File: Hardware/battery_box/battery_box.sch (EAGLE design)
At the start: 24 parts, among them IC1 LM2574N-5.0, U1 PIC16F506P

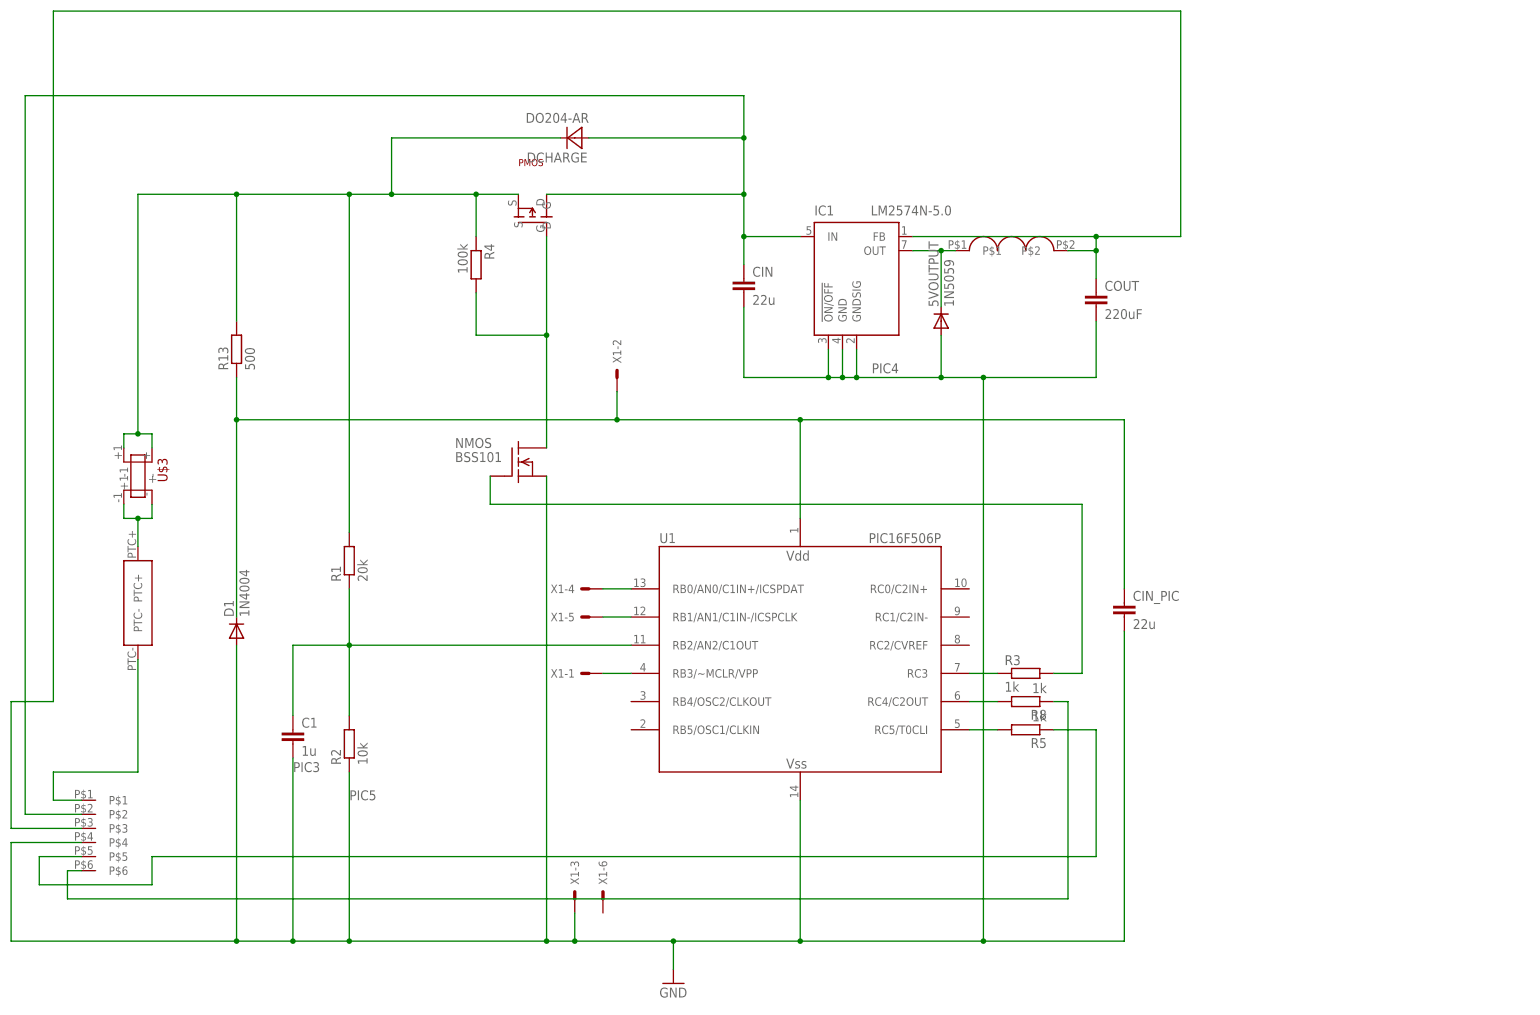
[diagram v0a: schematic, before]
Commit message: Added Connectors to Schematic
Adds the DC Jacks and USB connectors and LEDs to the schematic for
mounting on PCB. Added comments to schematic and changed .gitignore
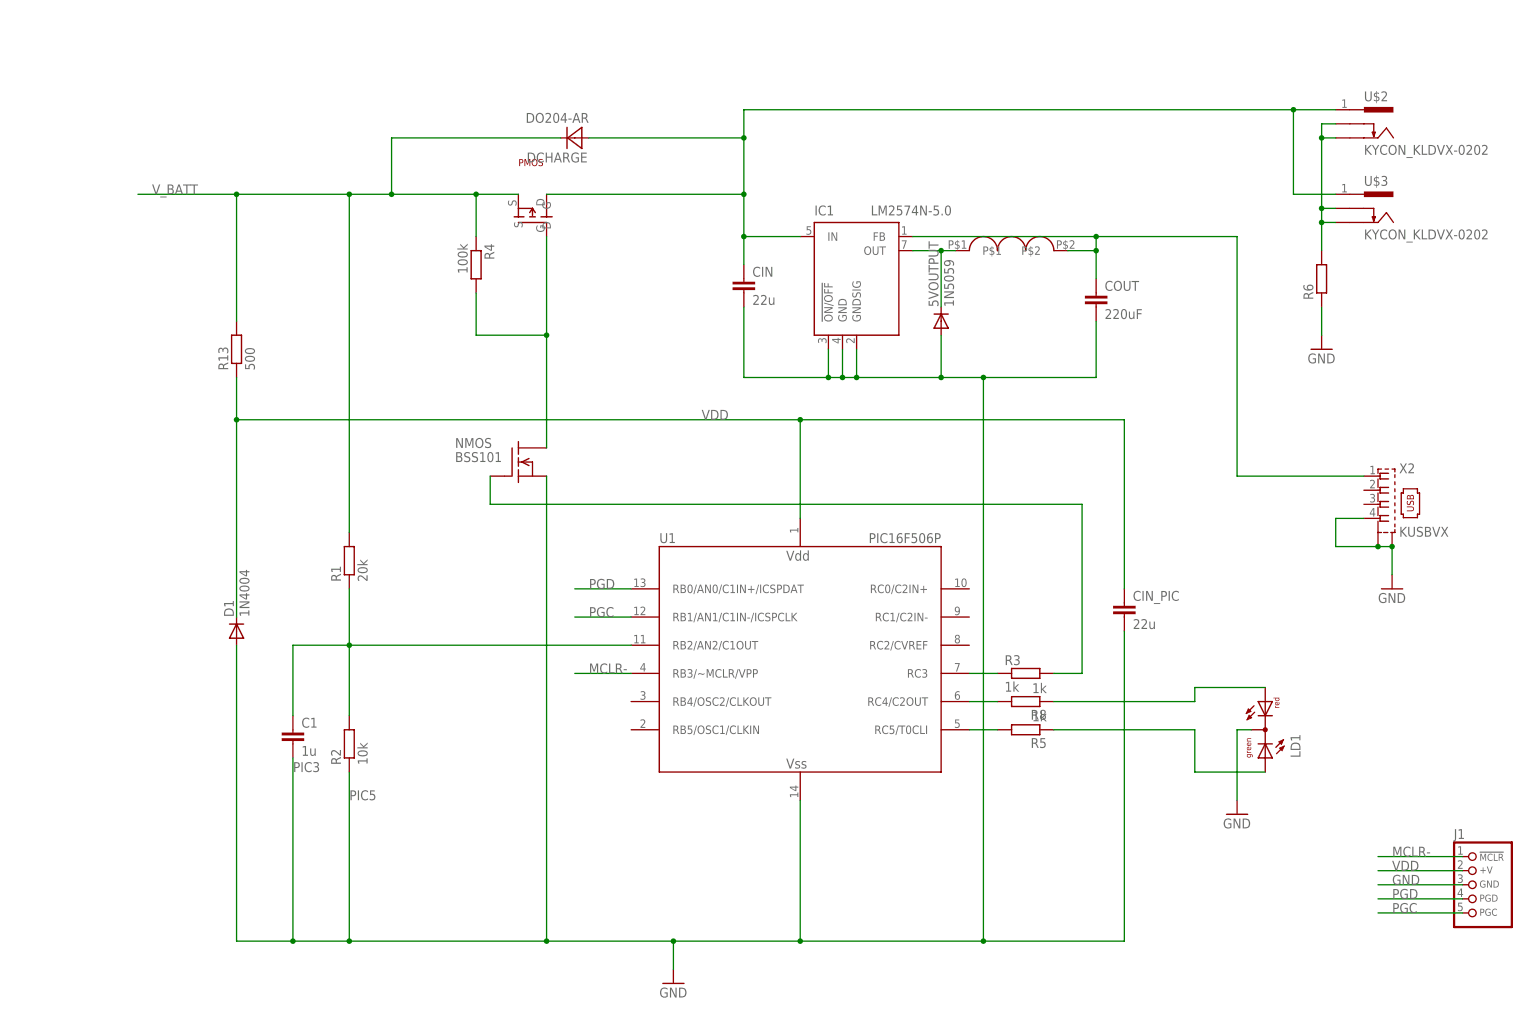
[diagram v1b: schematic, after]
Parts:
- removed TB: 6WAYTB, inverter:6WAYTB
- removed X1: (no value), con-molex:22-23-2061
- added J1: CON_HEADER_PRG_PIC_ICSPA, equinox:CON_HEADER_PRG_PIC_ICSPA
- added LD1: (no value), led:DUOLED-RG-C
- added R6: (no value), rcl:R-EU_R0805
- added X2: KUSBVX, con-kycon:KUSBVX
- U$2: value EQBX_PTCEQBX_PTC -> KYCON_KLDVX-0202; device eqbx_ptc:EQBX_PTCEQBX_PTC -> equinox:KYCON_KLDVX-0202
- U$3: value EQBX_FUSEEQBX_FUSE -> KYCON_KLDVX-0202; device eqbx_fuse:EQBX_FUSEEQBX_FUSE -> equinox:KYCON_KLDVX-0202
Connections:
- removed net N$10: U1.RB3/~MCLR/VPP, X1-1.S
- removed net N$14: R8.1, TB.P$6
- removed net N$19: TB.P$1, U$2.PTC-
- removed net N$5: U1.RB0/AN0/C1IN+/ICSPDAT, X1-4.S
- removed net N$6: CIN_PIC.1, D1.C, R13.1, U1.VDD, X1-2.S
- removed net N$7: U1.RB1/AN1/C1IN-/ICSPCLK, X1-5.S
- new net MCLR-: J1./MCLR, U1.RB3/~MCLR/VPP
- new net PGC: J1.PGC, U1.RB1/AN1/C1IN-/ICSPCLK
- new net PGD: J1.PGD, U1.RB0/AN0/C1IN+/ICSPDAT
- new net VDD: CIN_PIC.1, D1.C, J1.+V, R13.1, U1.VDD
- new net V_BATT: DCHARGE.C, PMOS.S, R1.2, R13.2, R4.1
- net GND: now also J1.GND, LD1.C, R6.1, X2.4, X2.S1, X2.S2; no longer TB.P$4, X1-3.S
- net N$1: now also R6.2, U$2.PAD2, U$2.PAD3, U$3.PAD2, U$3.PAD3; no longer U$2.PTC+, U$3.-, U$3.-1
- net N$17: now also LD1.AR, R8.1; no longer COUT.1, IC1.FB, INDUCTOR.P$2, TB.P$3
- net N$2: now also LD1.AG; no longer TB.P$5
- net N$20: now also U$2.PAD1, U$3.PAD1; no longer TB.P$2
- net N$4: now also COUT.1, IC1.FB, INDUCTOR.P$2, X2.1; no longer DCHARGE.C, PMOS.S, R1.2, R13.2, R4.1, U$3.+, U$3.+1
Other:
- note added: "Add Data Pin Bias"
- note added: "Current Sense R for Over-Current Protection"
- note added: "Switch to PIC16F1503"
- note added: "Use just 1 NMOS to switch"
- note removed: "PIC4"

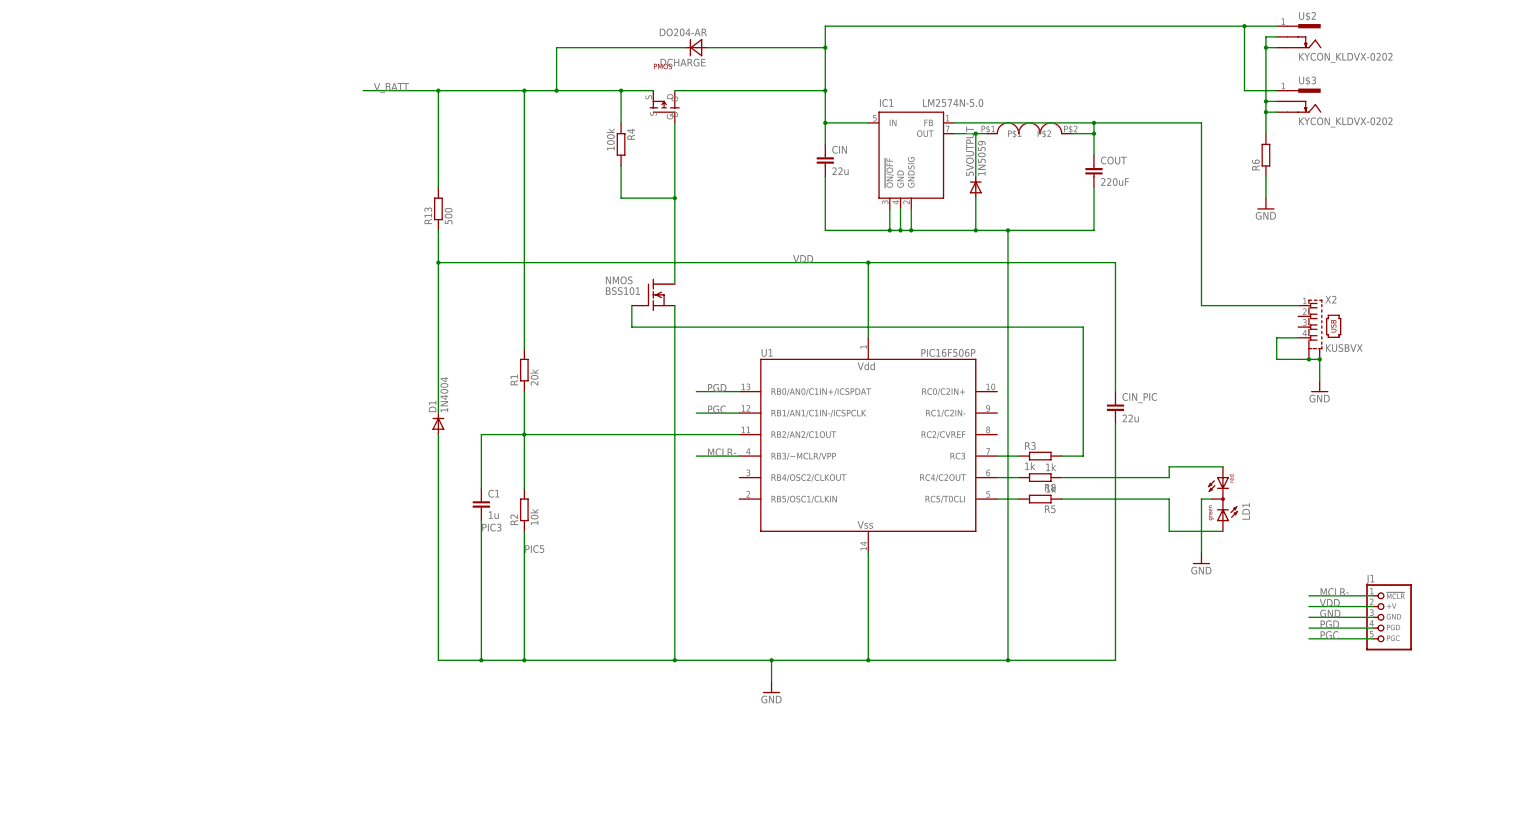
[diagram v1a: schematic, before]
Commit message: Added cooments to fix problems identified
Problems identified during 2013 Jan trip have added as comments.
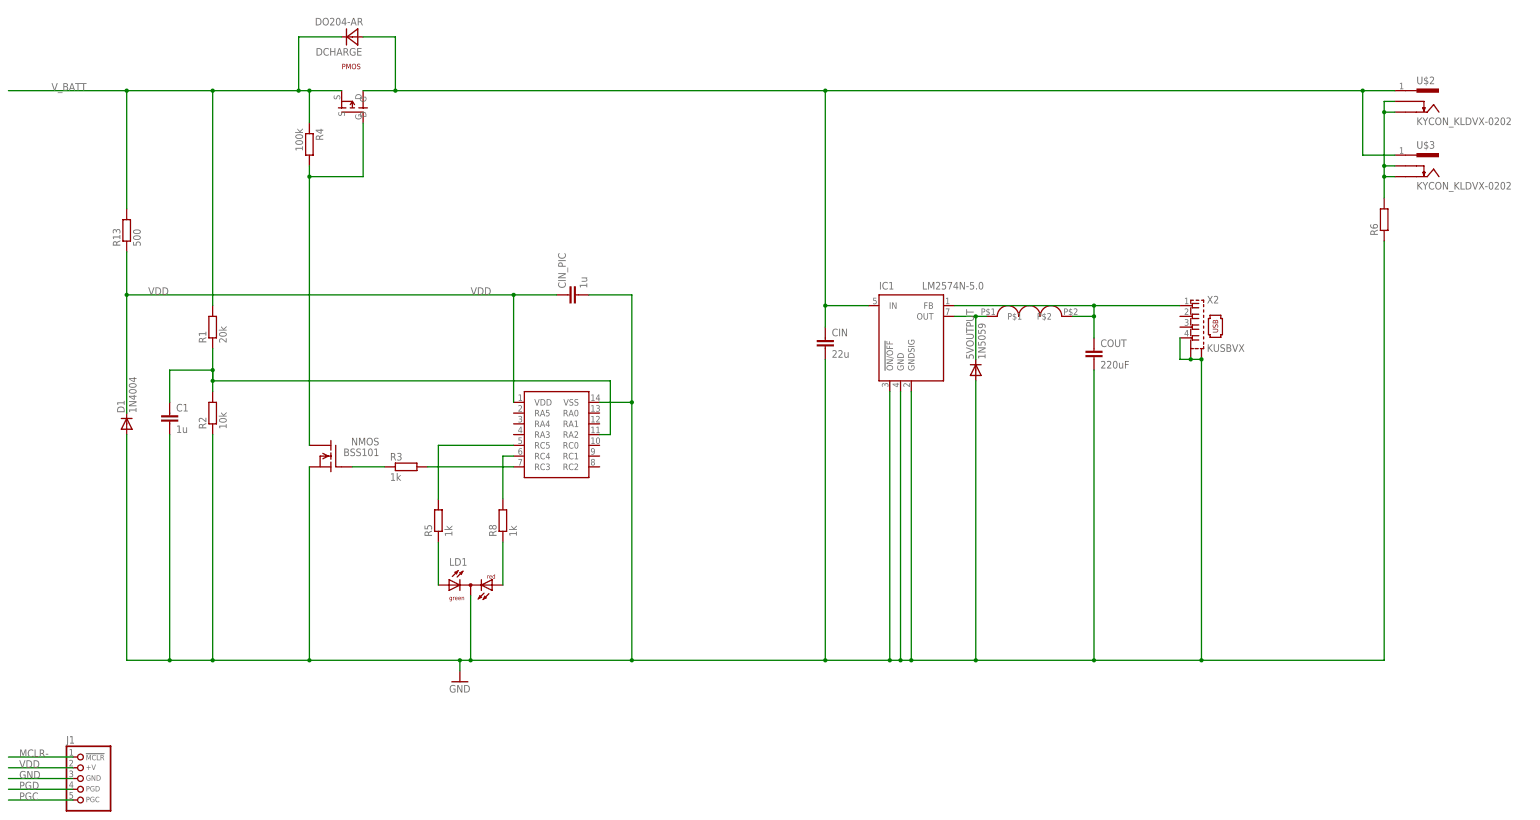
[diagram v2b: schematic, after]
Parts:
- removed U1: PIC16F506P, microchip:PIC16F506P
- added U$4: PIC16F1503SOIC, equinox:PIC16F1503SOIC
- C1: device capacitor-wima:C2.5/2 -> rcl:C-EUC0805
- CIN_PIC: value 22u -> 1u; device capacitor-wima:C2.5/2 -> rcl:C-EUC0805
- R1, R13, R2, R3, R4, R5, R8: device rcl:R-EU_0204/7 -> rcl:R-EU_R0805
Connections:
- removed net N$12: R3.1, U1.RC3
- new net N$5: R3.2, U$4.RC3
- net GND: now also U$4.VSS; no longer U1.VSS
- net MCLR-: no longer U1.RB3/~MCLR/VPP
- net N$13: now also R3.1; no longer R3.2
- net N$15: now also U$4.RC4; no longer U1.RC4/C2OUT
- net N$3: now also U$4.RA2; no longer U1.RB2/AN2/C1OUT
- net N$8: now also U$4.RC5; no longer U1.RC5/T0CLI
- net PGC: no longer U1.RB1/AN1/C1IN-/ICSPCLK
- net PGD: no longer U1.RB0/AN0/C1IN+/ICSPDAT
- net VDD: now also U$4.VDD; no longer U1.VDD
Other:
- note added: "Add EEPROM for latched LVDC"
- note added: "Add charging LED status"
- note added: "Add latched PTM switch with interupt from the uC to turn off after timeout or extreme LVDC"
- note added: "Add simple error checking to code"
- note added: "Change for low power voltage regulator"
- note added: "Check how the V_drop affects the charging off the battery. Possibly change how the charging works."
- note added: "Molex connector to crimped battery"
- note added: "Move Current sense to high-side with amplifier Needs to be able to sense reverse current"
- note added: "Use just 1 NMOS to switch and move to low side of 12 line. Also, connect on/off bar signal to chip output to control USB port"
- note removed: "PIC3"
- note removed: "PIC5"
- note removed: "Switch to PIC16F1503"
- note removed: "Use just 1 NMOS to switch"
- moved on the sheet: 5VOUTPUT, C1, CIN, CIN_PIC, COUT, D1, DCHARGE, IC1, J1, LD1, NMOS, PMOS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

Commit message: Added the Connector Test PCB
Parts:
- added U$5, U$6, U$7, U$8: PCB_MOUNT_RICHO, equinox:PCB_MOUNT_RICHO
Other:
- note added: "Add Voltage Sense to outputs to check for charging voltage"
- note added: "PCB Mounts"
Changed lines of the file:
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@@
 <part name="J1" library="equinox" deviceset="CON_HEADER_PRG_PIC_ICSP" device="A"/>
 <part name="U$4" library="equinox" deviceset="PIC16F1503" device="SOIC"/>
+<part name="U$5" library="equinox" deviceset="PCB_MOUNT_RICHO" device=""/>
+<part name="U$6" library="equinox" deviceset="PCB_MOUNT_RICHO" device=""/>
+<part name="U$7" library="equinox" deviceset="PCB_MOUNT_RICHO" device=""/>
+<part name="U$8" library="equinox" deviceset="PCB_MOUNT_RICHO" device=""/>
 </parts>
 <sheets>
@@
 off the battery. Possibly change how the
 charging works.</text>
+<text x="165.1" y="104.14" size="1.778" layer="98">Add Voltage Sense to outputs to check for charging voltage</text>
+<text x="93.98" y="-83.82" size="1.778" layer="98">PCB Mounts</text>
 </plain>
 <instances>
@@
 <instance part="J1" gate="J" x="-58.42" y="-71.12"/>
 <instance part="U$4" gate="G$1" x="53.34" y="7.62"/>
+<instance part="U$5" gate="G$1" x="99.06" y="-81.28"/>
+<instance part="U$6" gate="G$1" x="111.76" y="-81.28"/>
+<instance part="U$7" gate="G$1" x="124.46" y="-81.28"/>
+<instance part="U$8" gate="G$1" x="137.16" y="-81.28"/>
 </instances>
 <busses>

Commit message: Electronics added.
Should be first fully working prototype of 2013 unit. See README for
changes from 2012 version.
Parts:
- removed 5VOUTPUT: 1N5059, diode:1N5059
- removed CIN: 22u, capacitor-wima:C2.5/2
- removed CIN_PIC: 1u, rcl:C-EUC0805
- removed COUT: 220uF, capacitor-wima:C5/5.5
- removed DCHARGE: DO204-AR, diode:DO204-AR
- removed INDUCTOR: EQBX_INDUCTOR2, inductor:EQBX_INDUCTOR2
- removed NMOS: BSS101, transistor-fet:BSS101
- removed PMOS: PMOS, PMOS:PMOS
- added 12V_OUT_1, 12V_OUT_2: KYCON_KLDVX-0202, equinox:KYCON_KLDVX-0202
- added C2, C3, C4: 22u, rcl:C-EUC0805
- added D2: BAS40, diode:BAS40
- added DATA_OUT: (no value), con-lstb:MA04-1
- added L1: INDUCTOR, equinox:INDUCTOR
- added Q1: IRFR5505PBFTO252, equinox:IRFR5505PBFTO252
- added Q2: BSS123, transistor-small-signal:BSS123
- added R10, R19: 10k, rcl:R-EU_R0805
- added R11: 0.005, rcl:R-EU_R2512
- added R12: 100k, rcl:R-EU_R0805
- added R14, R15: 66k, rcl:R-EU_R0805
- added R16, R17, R7: 1k, rcl:R-EU_R0805
- added R18: 1M, rcl:R-EU_R0805
- added R9: 20k, rcl:R-EU_R0805
- added SW_POW: (no value), SparkFun:TAC_SWITCHPTH
- added X1: CON_MOLEX_39_29_1028, equinox:CON_MOLEX_39_29_1028
- C1: value 1u -> (none)
- D1: value 1N4004 -> 5.1V; device diode:1N4004 -> zetex:DSOD323
- IC1: value LM2574N-5.0 -> AD826R; device linear:LM2574N-5.0 -> analog-devices:AD826R
- R1: value 20k -> 75k
- R13: value 500 -> 100k
- R2: value 10k -> 49.9k
- R3: value 1k -> 75k
- R4: value 100k -> 49.9k
- R6: value (none) -> 1k
- R8: value 1k -> 500
- U$2: value KYCON_KLDVX-0202 -> PTC; device equinox:KYCON_KLDVX-0202 -> equinox:PTC
- U$3: value KYCON_KLDVX-0202 -> PIC16F1824; device equinox:KYCON_KLDVX-0202 -> equinox:PIC16F1824
- U$4: value PIC16F1503SOIC -> LM2574; device equinox:PIC16F1503SOIC -> equinox:LM2574
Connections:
- removed net MCLR-: J1./MCLR
- removed net N$13: NMOS.G, R3.1
- removed net N$4 (its old number): COUT.1, IC1.FB, INDUCTOR.P$2, X2.1
- new net I_SENSE: IC1A.OUT, R15.1, U$3.P$10
- new net MCLR_: J1./MCLR, U$3.P$4
- new net N$10: R5.2, U$3.P$8
- new net N$12: Q2.G, R6.1
- new net N$14: R6.2, U$3.P$7
- new net N$16: IC1A.IN-, R15.2, R17.2
- new net N$19: IC1B.IN-, IC1B.OUT, R14.2
- new net N$2: LD1.AR, R7.1
- new net N$6: U$2.P$1, X1CON$1.S
- new net N$7: R7.2, U$3.P$9
- new net POW: R19.1, SW_POW.1, SW_POW.2, U$3.P$2
- new net RX: DATA_OUT.3, U$3.P$5
- new net TX: DATA_OUT.2, U$3.P$6
- new net USB_OUT: C3.1, L1.P$2, R1.2, R3.2, U$4.FB, X2.1
- net GND: now also C4.2, DATA_OUT.1, IC1P.V-, Q2.S, R10.1, R11.1, R13.2, R17.1, SW_POW.3, SW_POW.4, U$3.P$14, X1CON$2.S; no longer 5VOUTPUT.A, CIN.2, CIN_PIC.2, COUT.2, IC1.!ON/OFF, IC1.GND@PWR, IC1.GNDSIG, NMOS.S, R2.1, R6.1, U$4.VSS, X2.4, X2.S1, X2.S2
- net N$1: now also 12V_OUT_1.PAD1, 12V_OUT_2.PAD1, C2.1, Q1.D, U$4.IN; no longer R6.2, U$2.PAD2, U$2.PAD3, U$3.PAD2, U$3.PAD3
- net N$11: now also Q1.G, Q2.D, R18.2; no longer 5VOUTPUT.C, IC1.OUT, INDUCTOR.P$1
- net N$15: now also IC1A.IN+, R14.1, R16.2; no longer R8.2, U$4.RC4
- net N$17: now also IC1B.IN+, R12.2, R13.1; no longer LD1.AR, R8.1
- net N$20: now also 12V_OUT_1.PAD2, 12V_OUT_1.PAD3, 12V_OUT_2.PAD2, 12V_OUT_2.PAD3, C2.2, C3.2, D2.A, R11.2, R16.1, R2.1, R4.1, U$4.ON/OFF, U$4.PWR_GND, U$4.SIG_GND, X2.4, X2.S1, X2.S2; no longer CIN.1, DCHARGE.A, IC1.IN, PMOS.D, U$2.PAD1, U$3.PAD1
- net N$3: now also X2.3; no longer C1.1, U$4.RA2
- net N$5: now also R3.1, R4.2, X2.2; no longer R3.2, U$4.RC3
- net N$8: now also C1.1, R10.2, R9.1, U$3.P$11; no longer R5.2, U$4.RC5
- net N$9: now also D2.C, L1.P$1, U$4.OUT; no longer NMOS.D, PMOS.G, R4.2
- net PGC: now also U$3.P$12
- net PGD: now also U$3.P$13
- net VDD: now also C4.1, DATA_OUT.4, IC1P.V+, R12.1, R19.2, R8.1, U$3.P$1; no longer CIN_PIC.1, R13.1, U$4.VDD
- net V_BATT: now also Q1.S, R18.1, R8.2, R9.2, U$2.P$2; no longer DCHARGE.C, PMOS.S, R1.2, R13.2, R4.1
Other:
- note added: "Added e.quinox logo"
- note added: "Change to 3.3V"
- note removed: "Add Data Pin Bias"
- note removed: "Add EEPROM for latched LVDC"
- note removed: "Add Voltage Sense to outputs to check for charging voltage"
- note removed: "Add charging LED status"
- note removed: "Add latched PTM switch with interupt from the uC to turn off after timeout or extreme LVDC"
- note removed: "Add simple error checking to code"
- note removed: "Check how the V_drop affects the charging off the battery. Possibly change how the charging works."
- note removed: "Current Sense R for Over-Current Protection"
- note removed: "Move Current sense to high-side with amplifier Needs to be able to sense reverse current"
- note removed: "Use just 1 NMOS to switch and move to low side of 12 line. Also, connect on/off bar signal to chip output to control USB port"
- moved on the sheet: C1, J1, LD1, R1, R13, R2, R3, R4, R5, R6, R8, X2

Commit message: Added comments to Schematic
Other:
- note added: "2069436"
- note added: "Need to change to cheaper op amp"
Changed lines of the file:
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@@
 <text x="294.64" y="27.94" size="1.778" layer="98">Added e.quinox logo</text>
 <text x="45.72" y="66.04" size="1.778" layer="98" rot="R90">Change to 3.3V</text>
+<text x="43.18" y="66.04" size="1.778" layer="98" rot="R90">2069436</text>
+<text x="190.5" y="116.84" size="3.81" layer="98">Need to change to cheaper op amp</text>
 </plain>
 <instances>

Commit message: Changed location op a mp power supply
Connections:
- net USB_OUT: now also IC1P.V+, R12.1
- net VDD: no longer IC1P.V+, R12.1
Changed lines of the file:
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@@
-</segment>
-<segment>
-<pinref part="IC1" gate="P" pin="V+"/>
-<wire x1="213.36" y1="106.68" x2="213.36" y2="111.76" width="0.1524" layer="91"/>
-<pinref part="R12" gate="G$1" pin="1"/>
-<wire x1="200.66" y1="111.76" x2="213.36" y2="111.76" width="0.1524" layer="91"/>
-<label x="203.2" y="111.76" size="1.778" layer="95"/>
 </segment>
 <segment>
@@
 <junction x="292.1" y="165.1"/>
 </segment>
+<segment>
+<pinref part="IC1" gate="P" pin="V+"/>
+<wire x1="213.36" y1="106.68" x2="213.36" y2="111.76" width="0.1524" layer="91"/>
+<pinref part="R12" gate="G$1" pin="1"/>
+<wire x1="200.66" y1="111.76" x2="213.36" y2="111.76" width="0.1524" layer="91"/>
+<label x="203.2" y="111.76" size="1.778" layer="95"/>
+</segment>
 </net>
